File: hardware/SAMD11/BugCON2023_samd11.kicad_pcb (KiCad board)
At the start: 2 copper layers, 122.4 x 97.9 mm, 28 parts, among them J1 Conn_01x04_Pin, J2 Conn_01x04_Pin, P1 USB_C_Plug_USB2.0, Q1 DMG3415U-7, SW1 SW_Push, SW2 ON, U1 ATSAMD11C14A-SS, U2 AP2112K-3.3

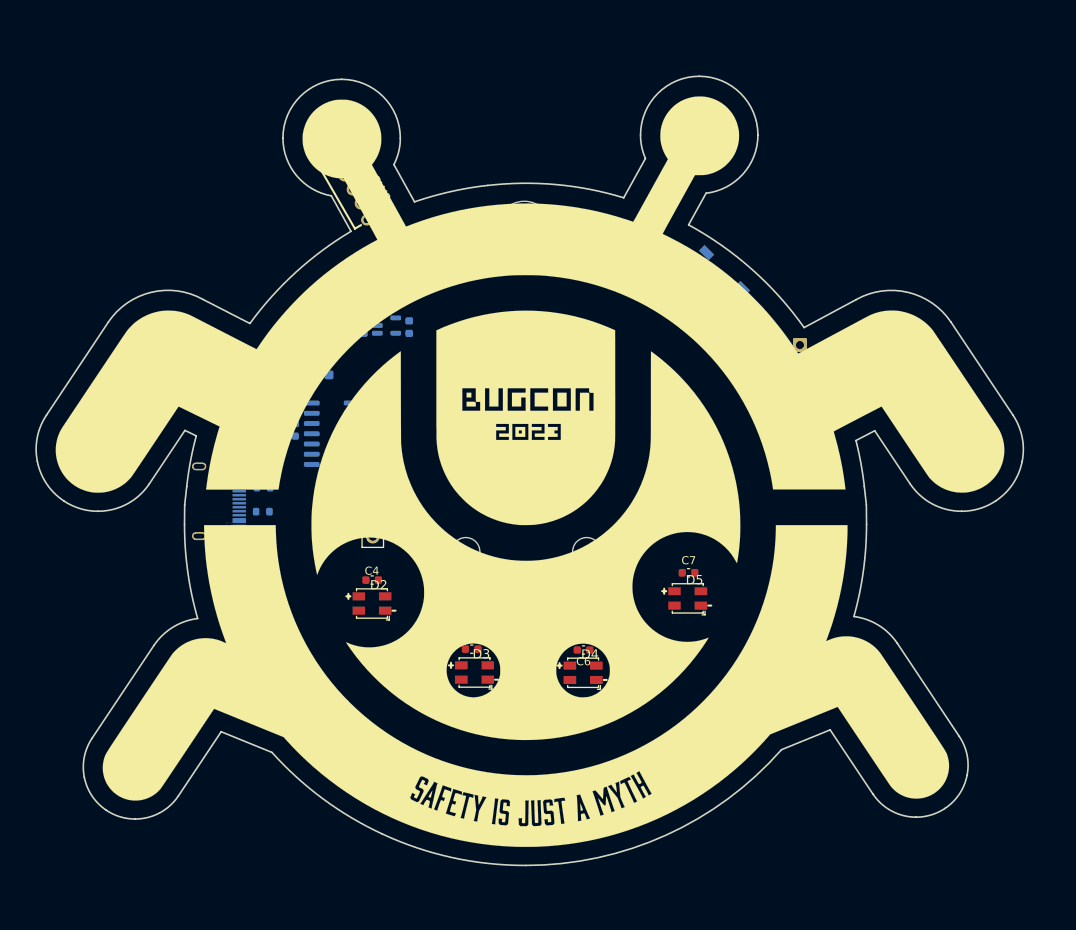
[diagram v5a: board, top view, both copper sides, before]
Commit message: upd routing and pad connector on samd11
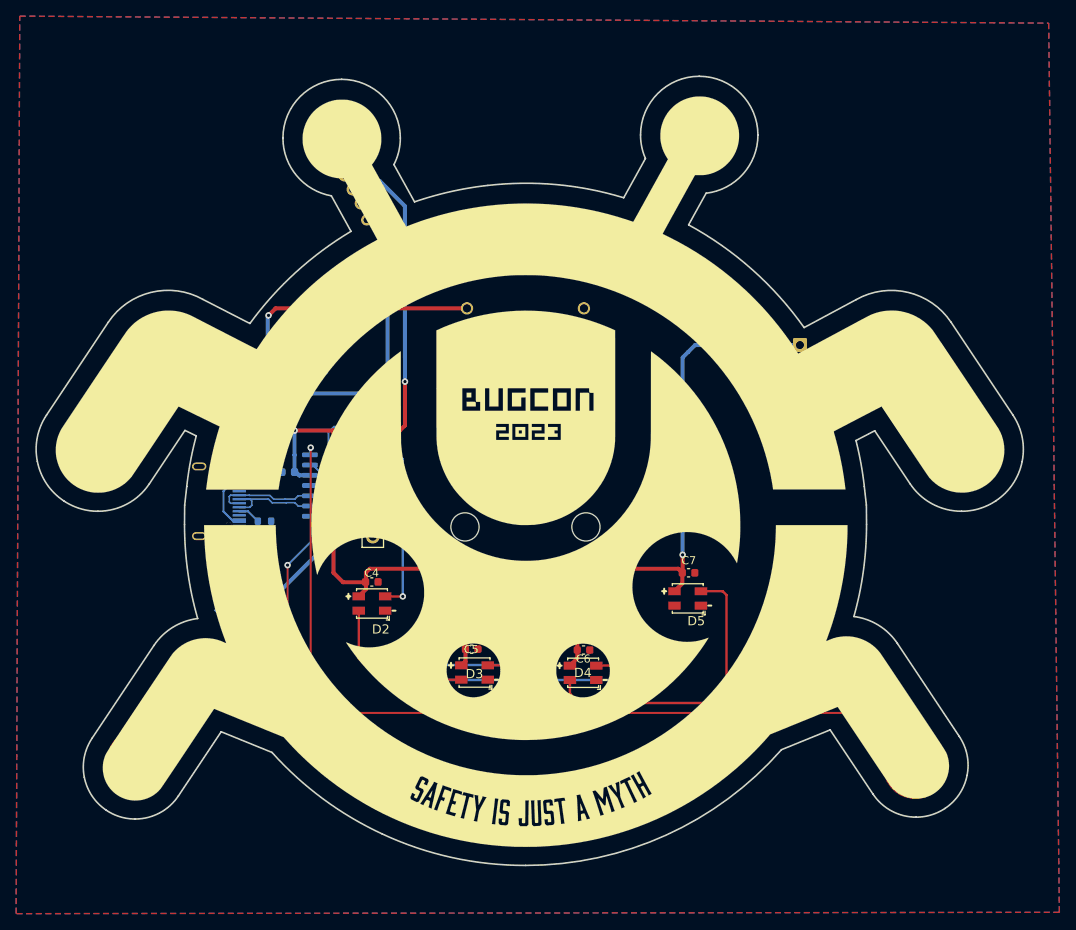
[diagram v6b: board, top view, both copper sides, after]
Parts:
- added J3: PAD2, BugCON2023_samd11:Piad, F.Cu at (102.6, 131.2)
- added J4: PAD, BugCON2023_samd11:Piad, F.Cu at (198.7, 132.0)
- added R5: 4.7, Resistor_SMD:R_0603_1608Metric, B.Cu at (131.4, 90.0)
- added R6: 4.7, Resistor_SMD:R_0603_1608Metric, B.Cu at (131.4, 91.5)
- SW2: moved to B.Cu
- moved SW1 71.1 mm to (116.3, 113.9)
- moved R4 25.3 mm to (131.4, 93.5), turned to 0 degrees
- moved C3 19.3 mm to (118.6, 85.9), turned to 180 degrees
- moved U2 18.6 mm to (118.4, 88.7), turned to 90 degrees
- moved C2 18.3 mm to (118.6, 91.5), turned to 180 degrees
- moved U1 6.42 mm to (126.2, 97.3)
- moved C1 5.30 mm to (121.1, 95.6), turned to 180 degrees
- moved D1 4.66 mm to (122.1, 84.5)
- moved Q1 4.45 mm to (118.5, 82.9), turned to 90 degrees
- moved R3 3.72 mm to (124.7, 83.0), turned to 0 degrees
- moved BT1 3.07 mm to (150.5, 102.4)
- moved F1 1.52 mm to (118.6, 94.4), turned to 90 degrees
- moved R1 1.20 mm to (118.1, 101.7)
- moved R2 0.56 mm to (118.4, 97.2)
- moved ? 0.40 mm to (150.3, 65.9)
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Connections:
- J2 pad 1: +3V3 -> +3.3V
- SW1 pad 1: +3.3V -> GND
- U1 pad 13: unconnected-(U1-PA02-Pad13) -> /IN2
- U1 pad 14: unconnected-(U1-PA04-Pad14) -> /IN1
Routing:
- net +3.3V: track 0.00 -> 209.7 mm, vias 0 -> 4
- net /IN1: track 0.00 -> 107.1 mm, vias 0 -> 1
- net Net-(D1-K): track 0.00 -> 47.7 mm, vias 0 -> 2
- net /IN2: track 0.00 -> 45.0 mm, vias 0 -> 1
- net Net-(D4-DOUT): track 0.00 -> 37.0 mm
- net +BATT: track 0.00 -> 30.8 mm, vias 0 -> 1
- net Net-(D2-DOUT): track 0.00 -> 26.9 mm, vias 0 -> 2
- net Net-(D3-DOUT): track 0.00 -> 26.7 mm, vias 0 -> 2
- net /RST: track 0.00 -> 25.6 mm
- net Net-(D2-DIN): track 0.00 -> 22.4 mm, vias 0 -> 1
- net /SCL: track 0.00 -> 17.6 mm
- net /SDA: track 0.00 -> 14.2 mm
- net /D-: track 0.00 -> 13.0 mm
- net /D+: track 0.00 -> 12.4 mm
- net Net-(F1-Pad1): track 0.00 -> 11.6 mm
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- added copper zone on B.Cu, net GND
- added copper zone on F.Cu, net GND

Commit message: add serial on SAMD11
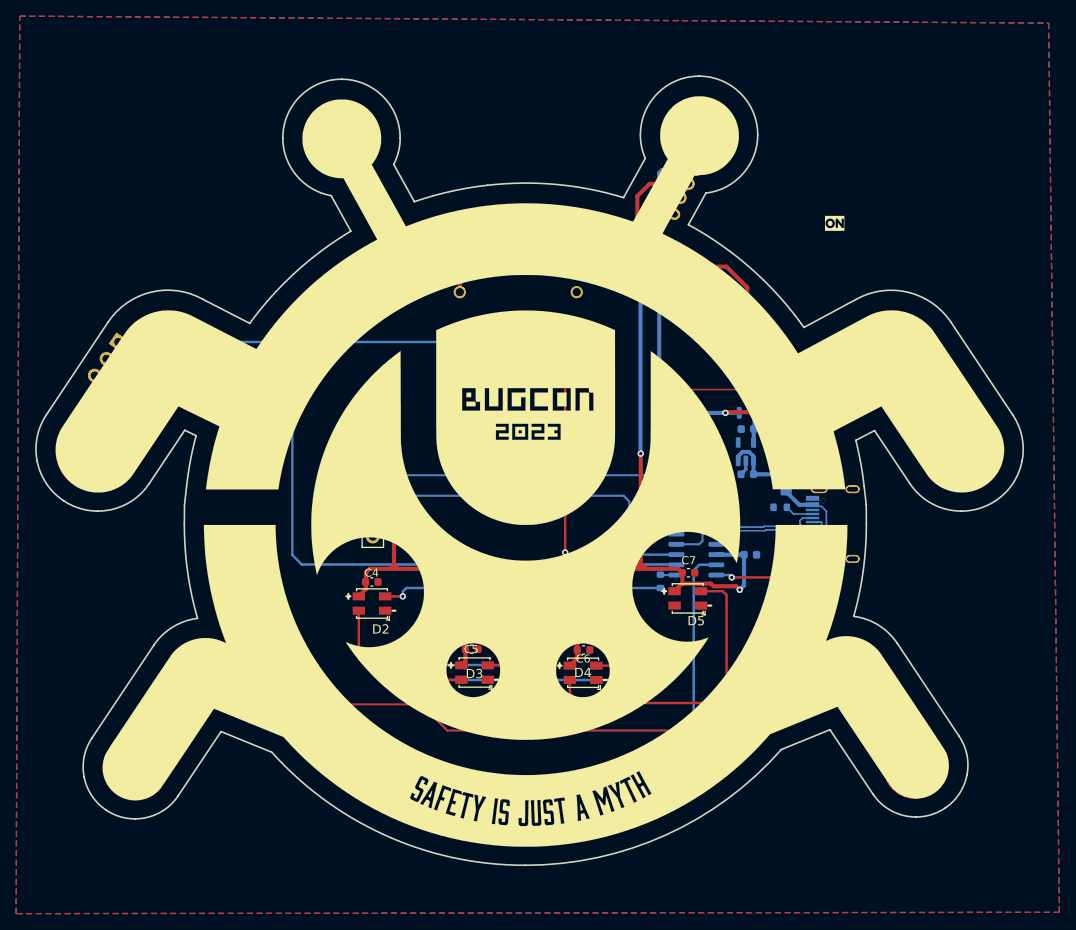
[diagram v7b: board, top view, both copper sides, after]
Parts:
- removed J2: Conn_01x04_Pin, Connector_PinSocket_2.54mm:PinSocket_1x04_P2.54mm_Vertical
- added JE: Serial, Connector_PinSocket_2.54mm:PinSocket_1x03_P2.54mm_Vertical, B.Cu at (100.0, 79.5)
- added kibuzzard-652DCDAF: G***, kibuzzard-652DCDAF, F.Cu at (188.8, 64.8)
- added kibuzzard-652DCDD3: G***, kibuzzard-652DCDD3, B.Cu at (168.4, 56.4)
- added kibuzzard-652DCDF1: G***, kibuzzard-652DCDF1, B.Cu at (165.9, 60.9)
- J1: value Conn_01x04_Pin -> I2C
- moved RST 90.6 mm to (204.5, 93.1), turned to 45 degrees
- moved P1 72.8 mm to (186.9, 102.0), turned to -90 degrees
- moved R2 65.0 mm to (182.9, 105.1), turned to 90 degrees
- moved F1 64.3 mm to (182.8, 97.1)
- moved R1 64.0 mm to (182.1, 100.0), turned to 0 degrees
- moved D1 59.6 mm to (181.5, 88.8)
- moved U2 59.6 mm to (177.8, 93.1)
- moved C3 59.6 mm to (178.0, 90.3)
- moved Q1 59.6 mm to (177.9, 87.3)
- moved R3 59.6 mm to (184.2, 87.4)
- moved C2 59.6 mm to (178.0, 95.9)
- moved C1 58.2 mm to (178.3, 105.8), turned to 0 degrees
- moved U1 46.0 mm to (171.7, 104.5), turned to 0 degrees
- moved SW2 41.7 mm to (170.7, 59.8), turned to -120 degrees
- moved R4 39.1 mm to (167.2, 109.1), turned to -90 degrees
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- renumbered SW1 to RST
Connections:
- J4 pad : (no net) -> /IN1
- U1 pad 2: unconnected-(U1-PA08/XIN-Pad2) -> /TX
- U1 pad 3: unconnected-(U1-PA09/XOUT-Pad3) -> /RX
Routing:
- net /RX: track 0.00 -> 95.4 mm, vias 0 -> 2
- net /TX: track 0.00 -> 94.6 mm
- net /IN1: track 107.1 -> 36.0 mm
- net /IN2: track 45.0 -> 94.0 mm
- net /SDA: track 14.2 -> 55.4 mm
- net /RST: track 25.6 -> 63.7 mm, vias 0 -> 2
- net +3.3V: track 209.7 -> 172.5 mm, vias 4 -> 3
- net /SCL: track 17.6 -> 44.3 mm
- net +BATT: track 30.8 -> 53.1 mm
- net Net-(D2-DIN): track 22.4 -> 34.9 mm
- net Net-(D1-K): track 47.7 -> 55.3 mm
- net /D-: track 13.0 -> 16.0 mm
- net /D+: track 12.4 -> 15.3 mm
- net VBUS: track 7.51 -> 9.28 mm
- net Net-(P1-CC): track 2.81 -> 3.53 mm
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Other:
- board text added: "GND"
- board text added: "RX"
- board text added: "TX"

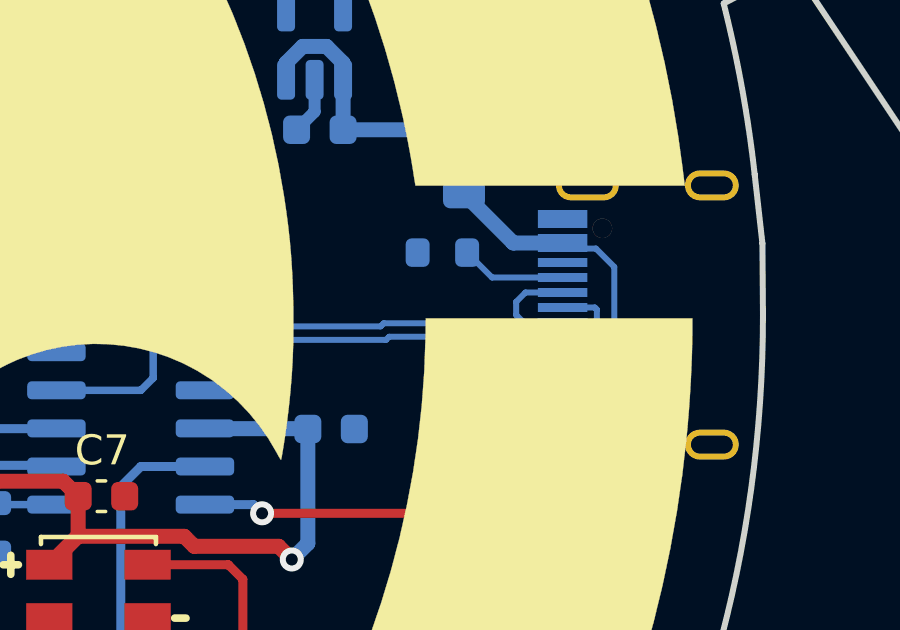
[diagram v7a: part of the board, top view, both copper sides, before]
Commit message: Change_footprint_USBC
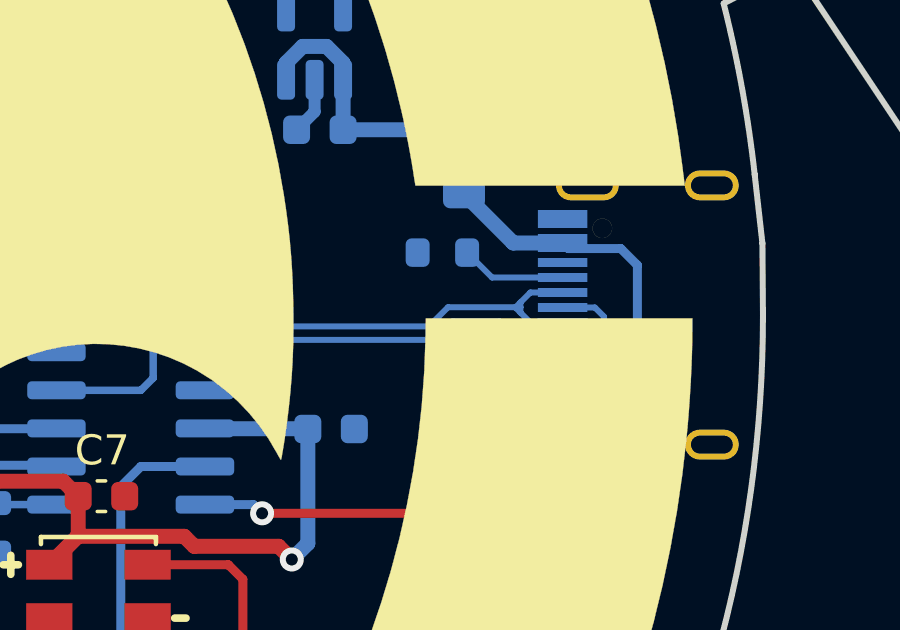
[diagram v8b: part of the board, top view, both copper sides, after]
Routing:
- net Net-(F1-Pad1): track 11.3 -> 13.0 mm
- net /D-: track 16.0 -> 14.8 mm
- net /D+: track 15.3 -> 16.0 mm
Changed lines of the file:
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@@
   (segment (start 178.75 93.638972) (end 178.198528 93.0875) (width 0.5) (layer "B.Cu") (net 5))
   (segment (start 182.5225 95.865) (end 182.78 96.1225) (width 0.5) (layer "B.Cu") (net 5))
-  (segment (start 187.1775 99.825) (end 186.2525 99.825) (width 0.2) (layer "B.Cu") (net 6))
-  (segment (start 187.79 100.4375) (end 187.1775 99.825) (width 0.2) (layer "B.Cu") (net 6))
-  (segment (start 187.1775 104.255) (end 187.79 103.6425) (width 0.2) (layer "B.Cu") (net 6))
+  (segment (start 186.2525 99.825) (end 186.0675 99.64) (width 0.3) (layer "B.Cu") (net 6))
+  (segment (start 188.005 99.825) (end 186.2525 99.825) (width 0.3) (layer "B.Cu") (net 6))
+  (segment (start 188.56 103.86) (end 188.56 100.38) (width 0.3) (layer "B.Cu") (net 6))
   (segment (start 184.4225 99.64) (end 182.78 97.9975) (width 0.5) (layer "B.Cu") (net 6))
-  (segment (start 186.2525 104.255) (end 187.1775 104.255) (width 0.2) (layer "B.Cu") (net 6))
-  (segment (start 187.79 103.6425) (end 187.79 100.4375) (width 0.2) (layer "B.Cu") (net 6))
-  (segment (start 186.0675 104.44) (end 186.2525 104.255) (width 0.2) (layer "B.Cu") (net 6))
+  (segment (start 186.0675 104.44) (end 186.2525 104.255) (width 0.3) (layer "B.Cu") (net 6))
+  (segment (start 188.56 100.38) (end 188.005 99.825) (width 0.3) (layer "B.Cu") (net 6))
+  (segment (start 186.2525 104.255) (end 188.165 104.255) (width 0.3) (layer "B.Cu") (net 6))
   (segment (start 186.0675 99.64) (end 184.4225 99.64) (width 0.5) (layer "B.Cu") (net 6))
-  (segment (start 186.2525 99.825) (end 186.0675 99.64) (width 0.2) (layer "B.Cu") (net 6))
+  (segment (start 188.165 104.255) (end 188.56 103.86) (width 0.3) (layer "B.Cu") (net 6))
   (segment (start 129.245 95.98) (end 131.54 95.98) (width 0.3) (layer "B.Cu") (net 7))
   (segment (start 171.73 95.98) (end 172.42 96.67) (width 0.25) (layer "B.Cu") (net 7))
@@
   (segment (start 186.0675 100.79) (end 183.715 100.79) (width 0.2) (layer "B.Cu") (net 12))
   (segment (start 183.715 100.79) (end 182.885 99.96) (width 0.2) (layer "B.Cu") (net 12))
-  (segment (start 187.21 101.8575) (end 187.1425 101.79) (width 0.2) (layer "B.Cu") (net 13))
-  (segment (start 187.1425 101.79) (end 186.0675 101.79) (width 0.2) (layer "B.Cu") (net 13))
-  (segment (start 187.07 102.79) (end 187.21 102.65) (width 0.2) (layer "B.Cu") (net 13))
   (segment (start 176.017501 102.87) (end 175.607501 103.28) (width 0.2) (layer "B.Cu") (net 13))
-  (segment (start 186.0675 102.79) (end 187.07 102.79) (width 0.2) (layer "B.Cu") (net 13))
-  (segment (start 184.804999 102.765) (end 180.285 102.765) (width 0.2) (layer "B.Cu") (net 13))
-  (segment (start 180.285 102.765) (end 180.18 102.87) (width 0.2) (layer "B.Cu") (net 13))
-  (segment (start 187.21 102.65) (end 187.21 101.8575) (width 0.2) (layer "B.Cu") (net 13))
-  (segment (start 186.0675 102.79) (end 184.829999 102.79) (width 0.2) (layer "B.Cu") (net 13))
+  (segment (start 186.0675 102.79) (end 184.5 102.79) (width 0.2) (layer "B.Cu") (net 13))
+  (segment (start 183.96 102.25) (end 182.415747 102.25) (width 0.2) (layer "B.Cu") (net 13))
+  (segment (start 187.1425 101.79) (end 187.45 102.0975) (width 0.2) (layer "B.Cu") (net 13))
+  (segment (start 184.5 102.79) (end 183.96 102.25) (width 0.2) (layer "B.Cu") (net 13))
+  (segment (start 182.415747 102.25) (end 181.795747 102.87) (width 0.2) (layer "B.Cu") (net 13))
   (segment (start 175.607501 103.28) (end 174.145 103.28) (width 0.2) (layer "B.Cu") (net 13))
-  (segment (start 184.829999 102.79) (end 184.804999 102.765) (width 0.2) (layer "B.Cu") (net 13))
-  (segment (start 180.18 102.87) (end 176.017501 102.87) (width 0.2) (layer "B.Cu") (net 13))
-  (segment (start 184.83 101.29) (end 184.52 101.6) (width 0.2) (layer "B.Cu") (net 14))
-  (segment (start 184.804999 102.315) (end 180.105 102.315) (width 0.2) (layer "B.Cu") (net 14))
+  (segment (start 187.1425 102.79) (end 186.0675 102.79) (width 0.2) (layer "B.Cu") (net 13))
+  (segment (start 181.795747 102.87) (end 176.017501 102.87) (width 0.2) (layer "B.Cu") (net 13))
+  (segment (start 186.0675 101.79) (end 187.1425 101.79) (width 0.2) (layer "B.Cu") (net 13))
+  (segment (start 187.45 102.4825) (end 187.1425 102.79) (width 0.2) (layer "B.Cu") (net 13))
+  (segment (start 187.45 102.0975) (end 187.45 102.4825) (width 0.2) (layer "B.Cu") (net 13))
+  (segment (start 184.9925 102.29) (end 184.66 101.9575) (width 0.2) (layer "B.Cu") (net 14))
+  (segment (start 175.607501 102.01) (end 174.145 102.01) (width 0.2) (layer "B.Cu") (net 14))
+  (segment (start 184.51 101.7725) (end 184.66 101.6225) (width 0.2) (layer "B.Cu") (net 14))
+  (segment (start 184.51 101.8075) (end 184.66 101.9575) (width 0.2) (layer "B.Cu") (net 14))
+  (segment (start 184.51 101.78) (end 184.51 101.7725) (width 0.2) (layer "B.Cu") (net 14))
+  (segment (start 184.9925 101.29) (end 186.0675 101.29) (width 0.2) (layer "B.Cu") (net 14))
+  (segment (start 184.66 101.78) (end 184.66 101.6225) (width 0.2) (layer "B.Cu") (net 14))
+  (segment (start 184.51 101.78) (end 182.249347 101.78) (width 0.2) (layer "B.Cu") (net 14))
+  (segment (start 186.0675 102.29) (end 184.9925 102.29) (width 0.2) (layer "B.Cu") (net 14))
+  (segment (start 184.66 101.6225) (end 184.9925 101.29) (width 0.2) (layer "B.Cu") (net 14))
+  (segment (start 184.66 101.9575) (end 184.66 101.78) (width 0.2) (layer "B.Cu") (net 14))
+  (segment (start 184.66 101.78) (end 184.51 101.78) (width 0.2) (layer "B.Cu") (net 14))
+  (segment (start 181.609347 102.42) (end 176.017501 102.42) (width 0.2) (layer "B.Cu") (net 14))
+  (segment (start 182.249347 101.78) (end 181.609347 102.42) (width 0.2) (layer "B.Cu") (net 14))
+  (segment (start 184.51 101.78) (end 184.51 101.8075) (width 0.2) (layer "B.Cu") (net 14))
   (segment (start 176.017501 102.42) (end 175.607501 102.01) (width 0.2) (layer "B.Cu") (net 14))
-  (segment (start 186.0675 102.29) (end 184.829999 102.29) (width 0.2) (layer "B.Cu") (net 14))
-  (segment (start 184.77 102.29) (end 186.0675 102.29) (width 0.2) (layer "B.Cu") (net 14))
-  (segment (start 180.105 102.315) (end 180 102.42) (width 0.2) (layer "B.Cu") (net 14))
-  (segment (start 184.52 102.04) (end 184.77 102.29) (width 0.2) (layer "B.Cu") (net 14))
-  (segment (start 186.0675 101.29) (end 184.83 101.29) (width 0.2) (layer "B.Cu") (net 14))
-  (segment (start 186.0675 102.29) (end 186.017501 102.339999) (width 0.2) (layer "B.Cu") (net 14))
-  (segment (start 180 102.42) (end 176.017501 102.42) (width 0.2) (layer "B.Cu") (net 14))
-  (segment (start 184.52 101.6) (end 184.52 102.04) (width 0.2) (layer "B.Cu") (net 14))
-  (segment (start 184.829999 102.29) (end 184.804999 102.315) (width 0.2) (layer "B.Cu") (net 14))
-  (segment (start 175.607501 102.01) (end 174.145 102.01) (width 0.2) (layer "B.Cu") (net 14))
   (segment (start 183.415 103.79) (end 182.95 104.255) (width 0.2) (layer "B.Cu") (net 15))
   (segment (start 186.0675 103.79) (end 183.415 103.79) (width 0.2) (layer "B.Cu") (net 15))
